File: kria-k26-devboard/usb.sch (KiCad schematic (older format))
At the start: 97 parts, among them U16 TPS2066TDGNRQ1, U17 USB7016_KDX, U18 TPS2066TDGNRQ1, U19 WE-TVS-82400152, U20 WE-TVS-82400152, U21 USB3310C-CP, U22 TPD4E05U06QDQARQ1, U23 TPD4E05U06QDQARQ1, U24 GSB3112311HR, U25 WE-TVS-82400152, U26 WE-TVS-82400152, U27 TPD4E05U06QDQARQ1, U28 TPD4E05U06QDQARQ1, U29 GSB3112311HR, Y4 ECS-2016MV-250-CN-TR3, Y5 ECS-2016MV-240-BN-TR3

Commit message: Finished PCB
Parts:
- added TP50, TP51: TP_SMD_0_75MM, antmicro-footprints:Testpoint_smd_0_75mm, symbol antmicroTestPoints:TP_SMD_0_75MM
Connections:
- net GND: no longer R62.1, R63.1
- net PS_3V3: now also R62.1, R63.1
- net at R62.2, U17.75 (PF26): now also TP50.1
- net at R63.2, U17.76 (PF27): now also TP51.1
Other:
- note added: "Slave SMBus"
- moved on the sheet: R62, R63
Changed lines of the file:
@@
 Wire Wire Line
 	2900 4400 2900 4500
-Wire Wire Line
-	7650 7400 7600 7400
-Wire Wire Line
-	7950 7400 8200 7400
 $Comp
 L antmicroResistors0402:R_200k_0402 R63
 U 1 1 64B39C27
-P 7800 7400
-F 0 "R63" H 7600 7450 60  0000 C CNN
-F 1 "R_200k_0402" H 7800 7250 60  0001 C CNN
-F 2 "antmicro-footprints:0402-res" H 8000 7600 60  0001 L CNN
-F 3 "" H 7800 7400 50  0001 C CNN
-F 4 "YAGEO_(PHYCOMP)" H 8000 7800 60  0001 L CNN "Manufacturer"
-F 5 "RC0402FR-07200KL" H 8000 7700 60  0001 L CNN "MPN"
-F 6 "200k" H 7800 7400 50  0000 C CNN "Val"
-	1    7800 7400
-	-1   0    0    1
-$EndComp
-Wire Wire Line
-	7650 7300 7600 7300
-Wire Wire Line
-	7950 7300 8200 7300
+P 8450 7050
+F 0 "R63" H 8250 7100 60  0000 C CNN
+F 1 "R_200k_0402" H 8450 6900 60  0001 C CNN
+F 2 "antmicro-footprints:0402-res" H 8650 7250 60  0001 L CNN
+F 3 "" H 8450 7050 50  0001 C CNN
+F 4 "YAGEO_(PHYCOMP)" H 8650 7450 60  0001 L CNN "Manufacturer"
+F 5 "RC0402FR-07200KL" H 8650 7350 60  0001 L CNN "MPN"
+F 6 "200k" H 8450 7050 50  0000 C CNN "Val"
+	1    8450 7050
+	0    1    1    0
+$EndComp
 $Comp
 L antmicroResistors0402:R_200k_0402 R62
 U 1 1 64B39C36
-P 7800 7300
-F 0 "R62" H 7600 7350 60  0000 C CNN
-F 1 "R_200k_0402" H 7800 7150 60  0001 C CNN
-F 2 "antmicro-footprints:0402-res" H 8000 7500 60  0001 L CNN
-F 3 "" H 7800 7300 50  0001 C CNN
-F 4 "YAGEO_(PHYCOMP)" H 8000 7700 60  0001 L CNN "Manufacturer"
-F 5 "RC0402FR-07200KL" H 8000 7600 60  0001 L CNN "MPN"
-F 6 "200k" H 7800 7300 50  0000 C CNN "Val"
-	1    7800 7300
-	-1   0    0    1
-$EndComp
-Wire Wire Line
-	8200 7300 8200 7400
-Wire Wire Line
-	8200 7600 8200 7400
-Connection ~ 8200 7400
+P 8350 7050
+F 0 "R62" H 8150 7100 60  0000 C CNN
+F 1 "R_200k_0402" H 8350 6900 60  0001 C CNN
+F 2 "antmicro-footprints:0402-res" H 8550 7250 60  0001 L CNN
+F 3 "" H 8350 7050 50  0001 C CNN
+F 4 "YAGEO_(PHYCOMP)" H 8550 7450 60  0001 L CNN "Manufacturer"
+F 5 "RC0402FR-07200KL" H 8550 7350 60  0001 L CNN "MPN"
+F 6 "200k" H 8350 7050 50  0000 C CNN "Val"
+	1    8350 7050
+	0    1    1    0
+$EndComp
 Wire Wire Line
 	8200 7700 8200 7600
@@
 	8200 7800 8200 7700
 Connection ~ 8200 7700
-Wire Wire Line
-	8200 6100 8200 7300
 Connection ~ 8200 6100
-Connection ~ 8200 7300
 Wire Wire Line
 	7600 4950 7750 4950
@@
 Wire Wire Line
 	900  2200 650  2200
-Wire Bus Line
-	10400 1100 10400 2350
 Text HLabel 7750 4950 2    50   Input ~ 0
 USB5_P
 Text HLabel 7750 5050 2    50   Input ~ 0
 USB5_N
+Text GLabel 8400 6650 1    50   Input ~ 0
+PS_3V3
+Wire Wire Line
+	8200 6100 8200 7600
+$Comp
+L antmicroTestPoints:TP_SMD_0_75MM TP50
+U 1 1 6293828A
+P 8650 7300
+F 0 "TP50" V 8750 7300 50  0000 L CNN
+F 1 "TP_SMD_0_75MM" H 8650 7200 50  0001 C CNN
+F 2 "antmicro-footprints:Testpoint_smd_0_75mm" H 8850 7500 60  0001 L CNN
+F 3 "" H 8850 7600 60  0001 L CNN
+	1    8650 7300
+	0    -1   -1   0
+$EndComp
+Wire Wire Line
+	7600 7300 8350 7300
+Wire Wire Line
+	8350 7300 8350 7200
+Wire Wire Line
+	7600 7400 8450 7400
+Wire Wire Line
+	8450 7400 8450 7200
+Wire Wire Line
+	8350 6900 8350 6700
+Wire Wire Line
+	8350 6700 8400 6700
+Wire Wire Line
+	8450 6700 8450 6900
+Wire Wire Line
+	8400 6700 8400 6650
+Connection ~ 8400 6700
+Wire Wire Line
+	8400 6700 8450 6700
+$Comp
+L antmicroTestPoints:TP_SMD_0_75MM TP51
+U 1 1 62D35A30
+P 8650 7400
+F 0 "TP51" V 8550 7400 50  0000 L CNN
+F 1 "TP_SMD_0_75MM" H 8650 7300 50  0001 C CNN
+F 2 "antmicro-footprints:Testpoint_smd_0_75mm" H 8850 7600 60  0001 L CNN
+F 3 "" H 8850 7700 60  0001 L CNN
+	1    8650 7400
+	0    -1   -1   0
+$EndComp
+Wire Wire Line
+	8350 7300 8550 7300
+Connection ~ 8350 7300
+Wire Wire Line
+	8450 7400 8550 7400
+Wire Bus Line
+	10400 1100 10400 2350
+Connection ~ 8450 7400
+Text Notes 8350 7650 0    50   ~ 0
+Slave SMBus
 $EndSCHEMATC

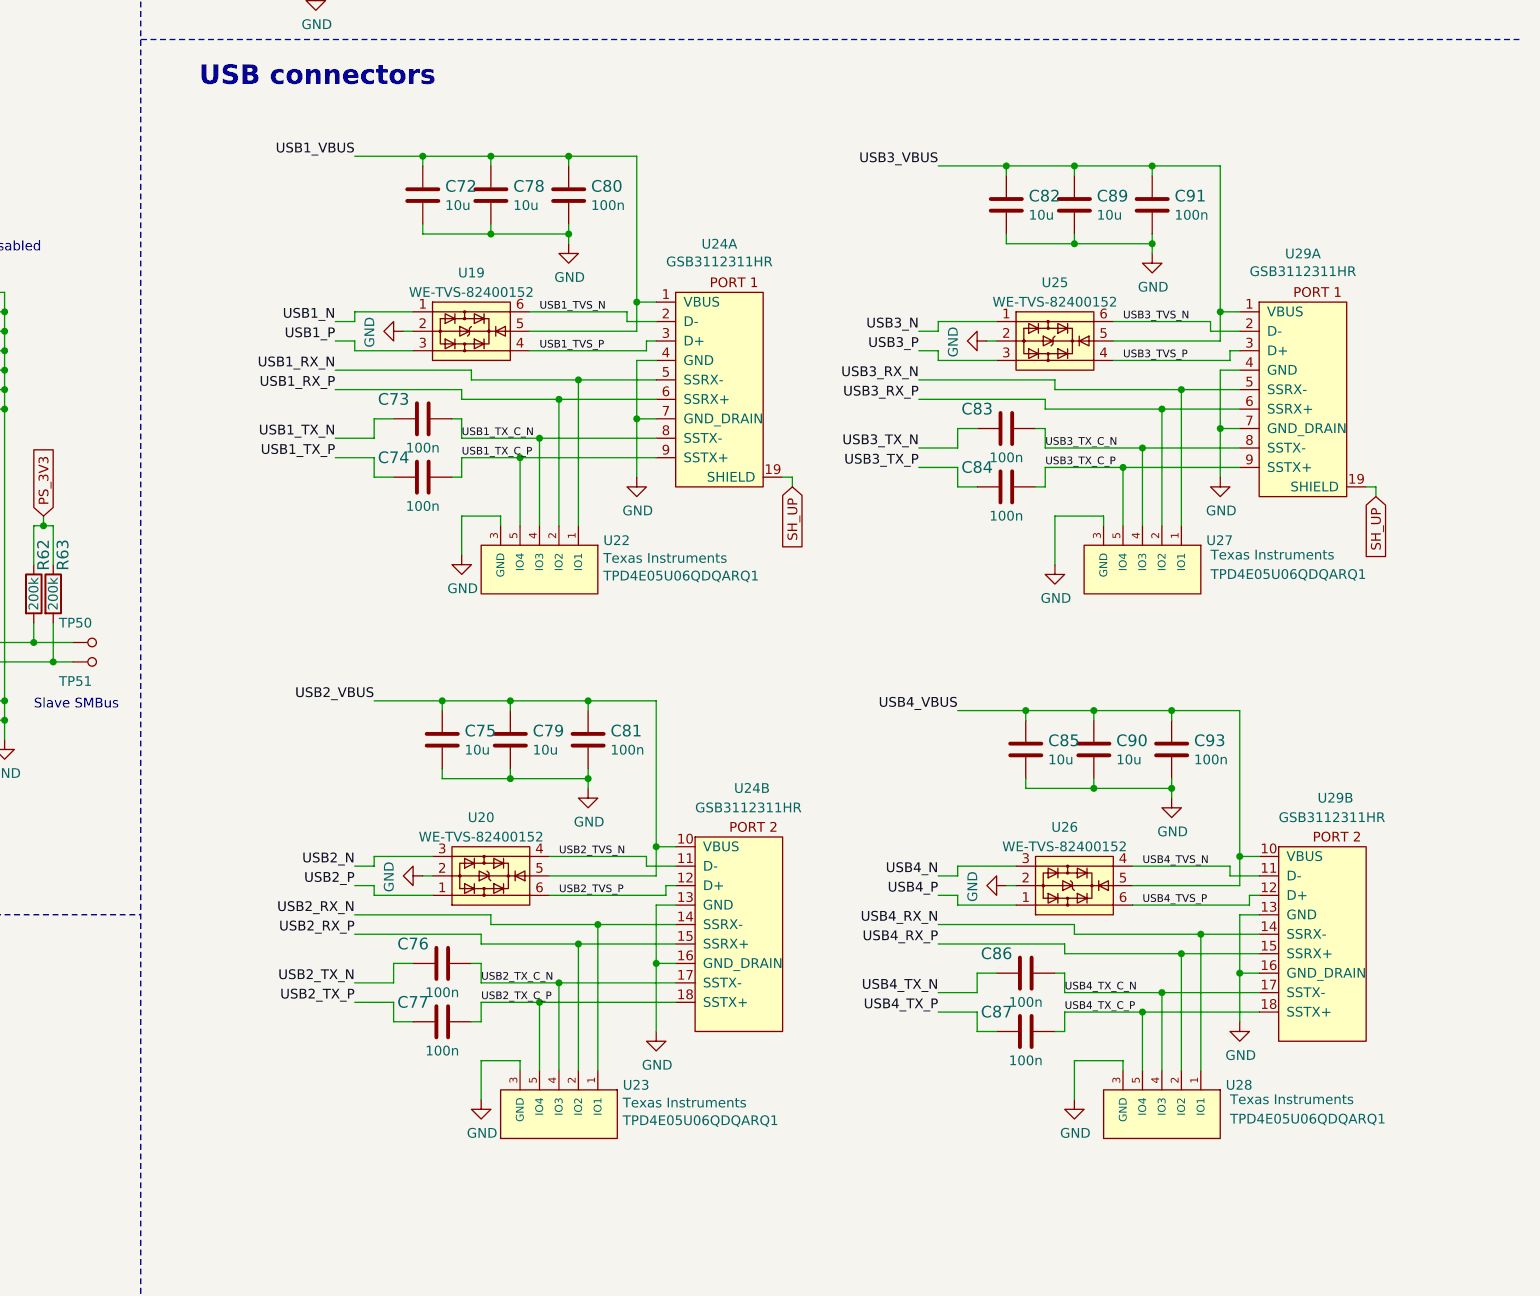
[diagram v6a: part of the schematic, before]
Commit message: Modified TPD4E05U06QDQARQ1 symbol to avoid misconnections on the schematic
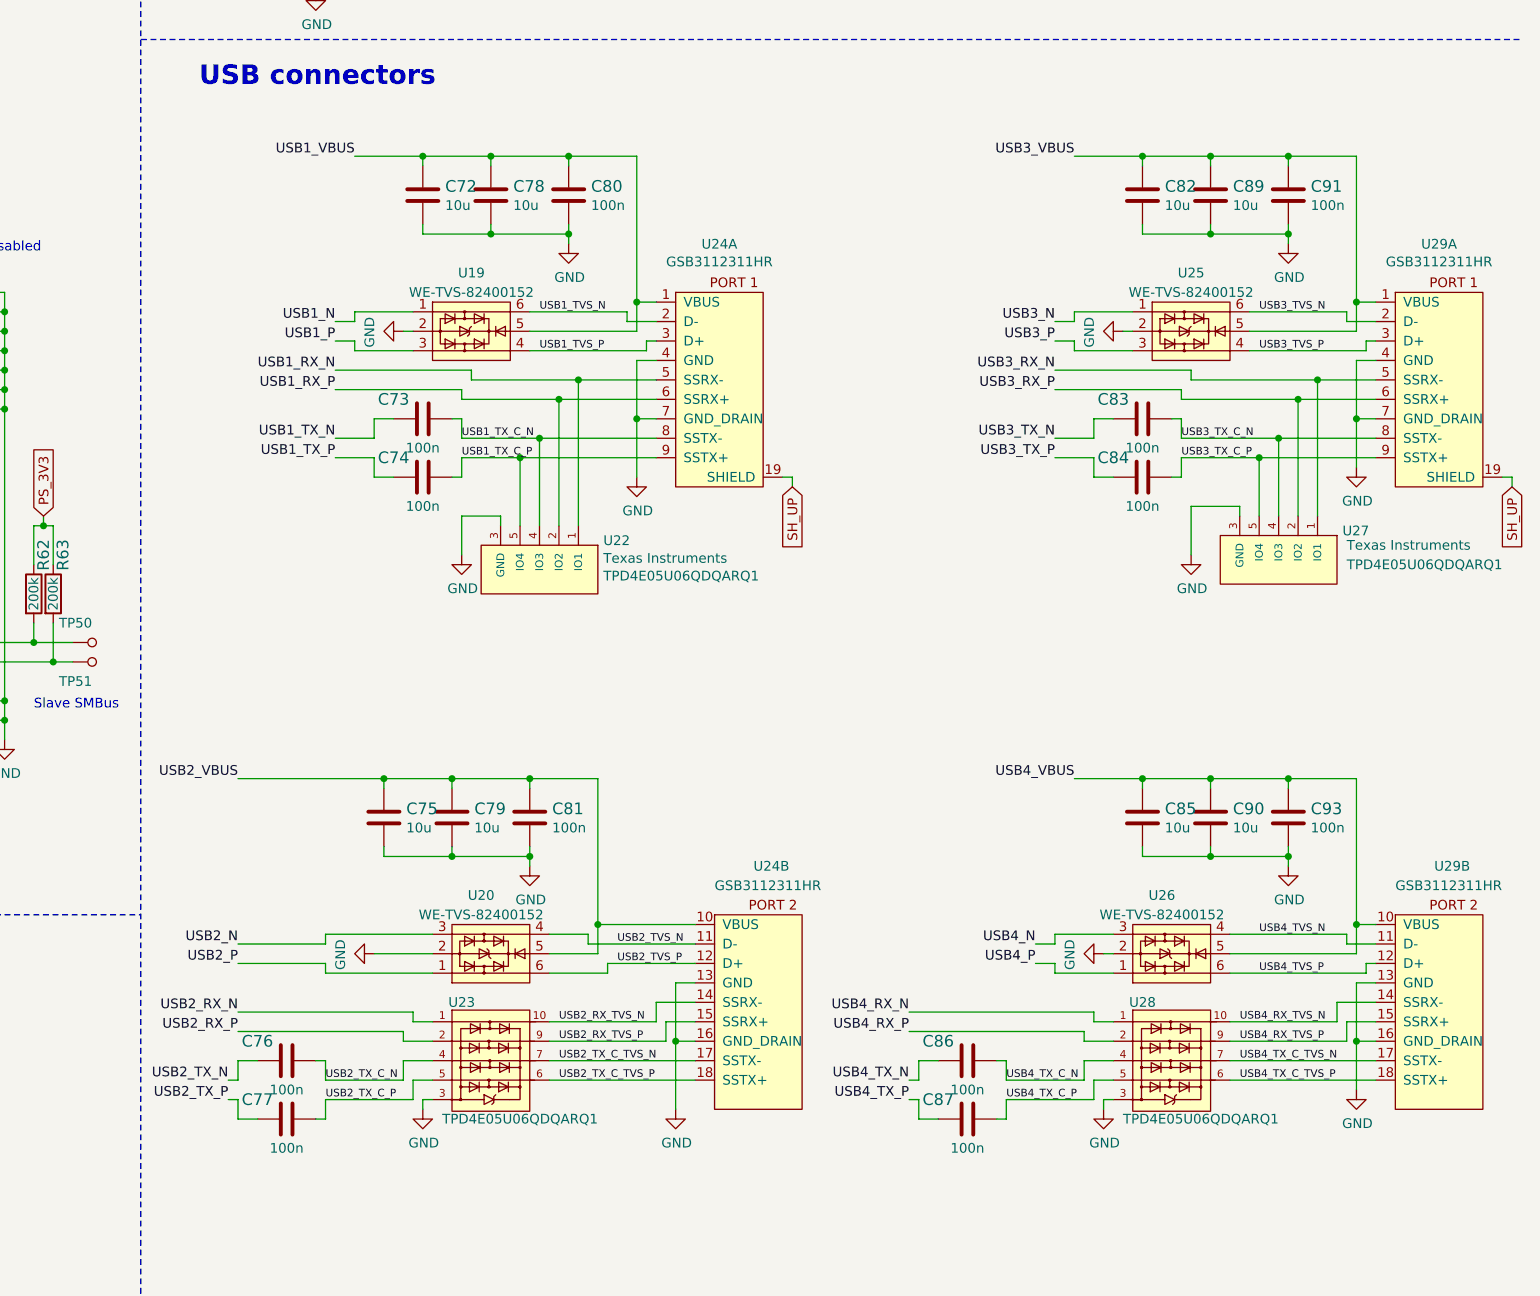
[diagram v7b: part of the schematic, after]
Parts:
- removed U23, U28: TPD4E05U06QDQARQ1, antmicro-footprints:TPD4E05U06QDQARQ1, symbol antmicroTVSDiodes:TPD4E05U06QDQARQ1
- added U23, U28: TPD4E05U06QDQARQ1_PASS, antmicro-footprints:TPD4E05U06QDQARQ1, symbol antmicroTVSDiodes:TPD4E05U06QDQARQ1_PASS
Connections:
- net GND: now also U23.3, U23.8 (GND), U28.3, U28.8 (GND)
- net USB2_RX_N: now also U23.1; no longer U24.14 (SSRX-)
- net USB2_RX_P: now also U23.2; no longer U24.15 (SSRX+)
- net USB2_TX_C_N: now also U23.4; no longer U24.17 (SSTX-)
- net USB2_TX_C_P: now also U23.5; no longer U24.18 (SSTX+)
- net USB4_RX_N: now also U28.1; no longer U29.14 (SSRX-)
- net USB4_RX_P: now also U28.2; no longer U29.15 (SSRX+)
- net USB4_TX_C_N: now also U28.4; no longer U29.17 (SSTX-)
- net USB4_TX_C_P: now also U28.5; no longer U29.18 (SSTX+)
- new net USB2_RX_TVS_N: U23.10, U24.14 (SSRX-)
- new net USB2_RX_TVS_P: U23.9, U24.15 (SSRX+)
- new net USB2_TX_C_TVS_N: U23.7, U24.17 (SSTX-)
- new net USB2_TX_C_TVS_P: U23.6, U24.18 (SSTX+)
- new net USB4_RX_TVS_N: U28.10, U29.14 (SSRX-)
- new net USB4_RX_TVS_P: U28.9, U29.15 (SSRX+)
- new net USB4_TX_C_TVS_N: U28.7, U29.17 (SSTX-)
- new net USB4_TX_C_TVS_P: U28.6, U29.18 (SSTX+)
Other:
- moved on the sheet: C75, C76, C77, C79, C81, C82, C83, C84, C85, C86, C87, C89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

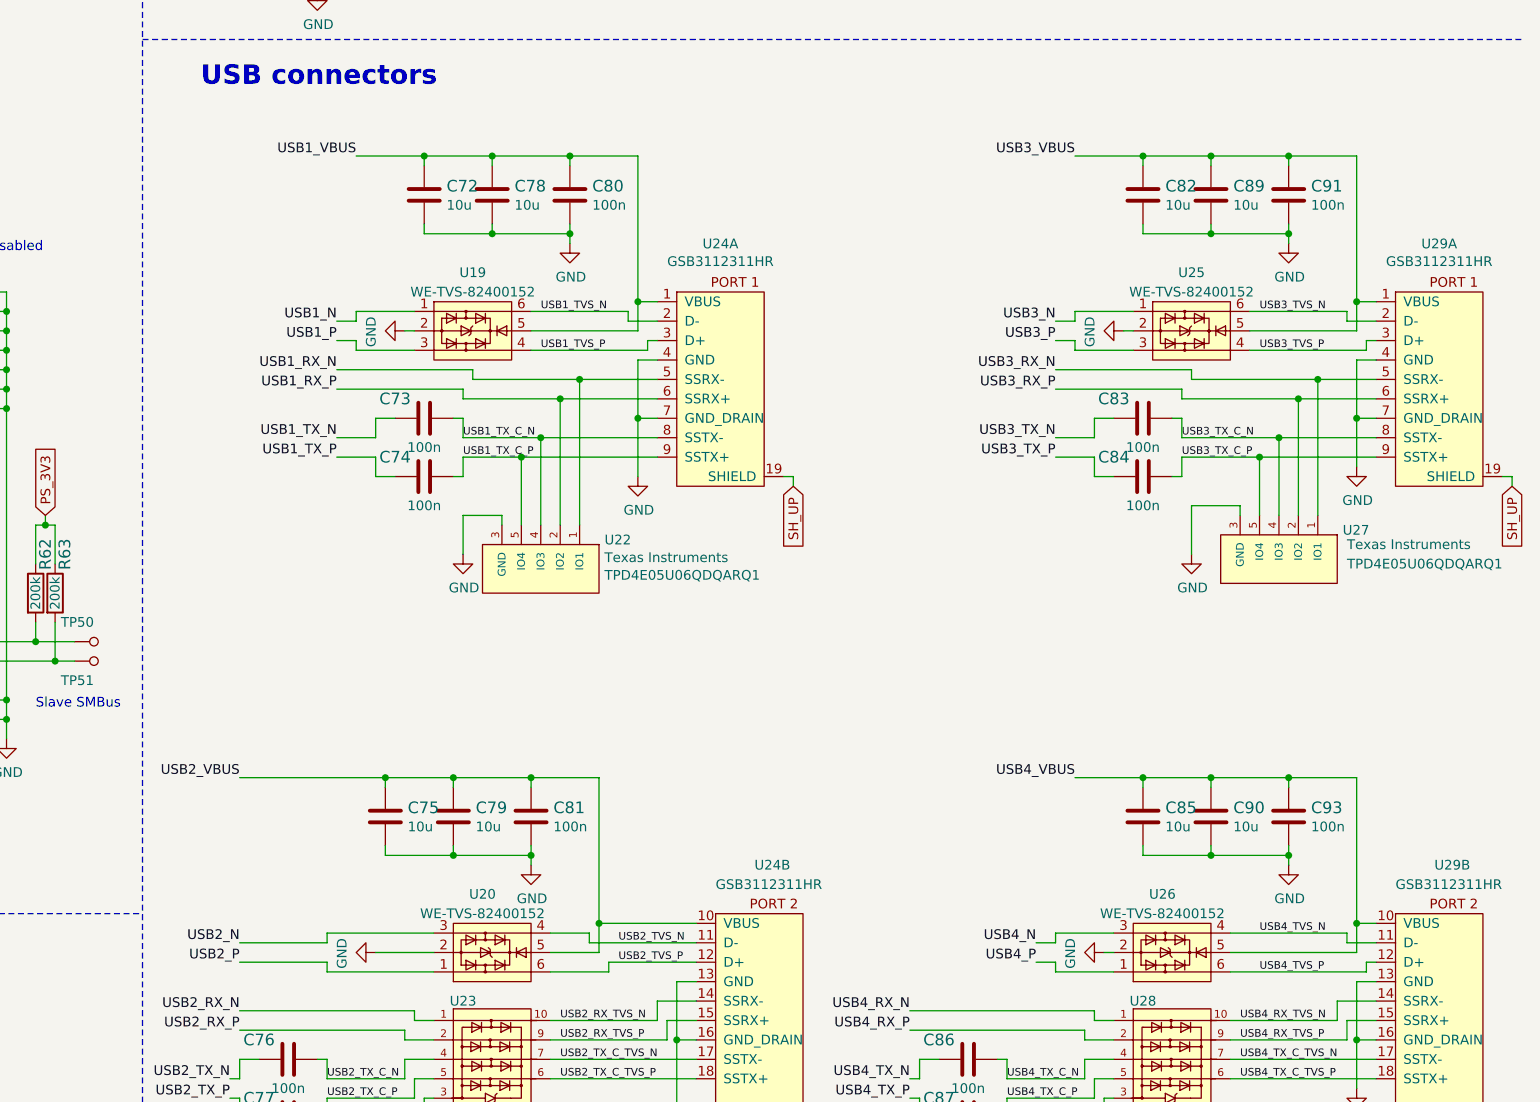
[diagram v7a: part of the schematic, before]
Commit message: Fixes introduced after initial review, length matching double checked with external plugin
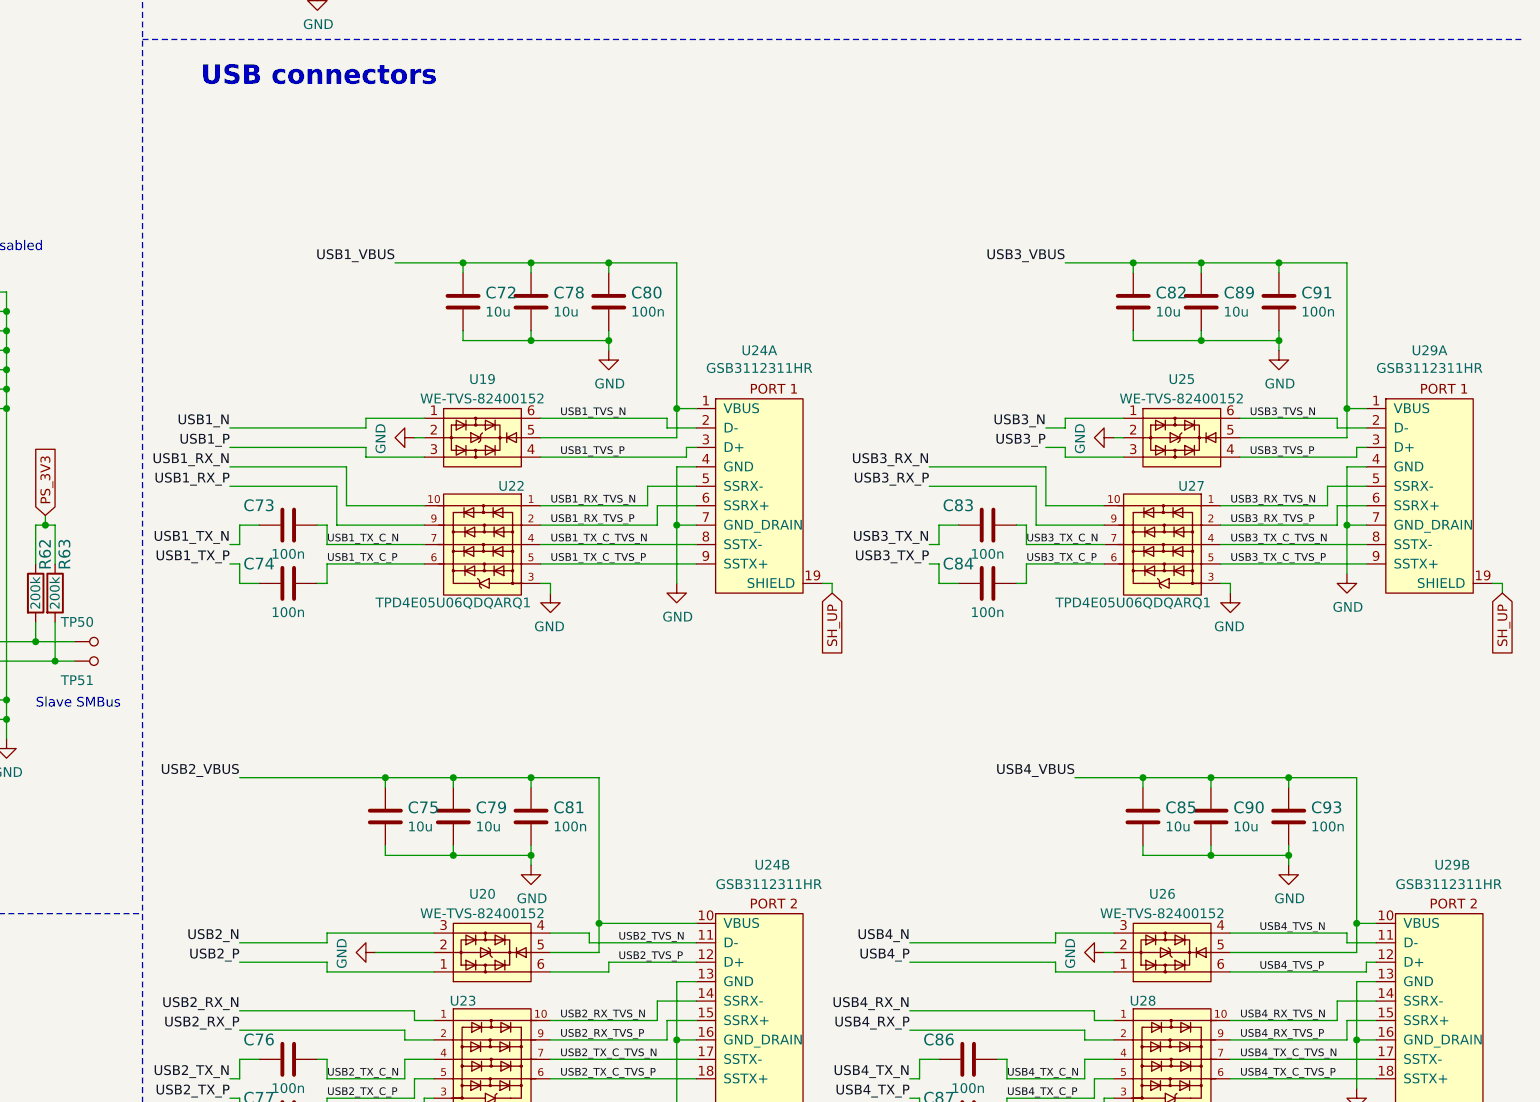
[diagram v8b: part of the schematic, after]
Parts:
- removed U22, U27: TPD4E05U06QDQARQ1, antmicro-footprints:TPD4E05U06QDQARQ1, symbol antmicroTVSDiodes:TPD4E05U06QDQARQ1
- added U22, U27: TPD4E05U06QDQARQ1_PASS, antmicro-footprints:TPD4E05U06QDQARQ1, symbol antmicroTVSDiodes:TPD4E05U06QDQARQ1_PASS
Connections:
- net GND: now also U22.3, U22.8 (GND), U27.3, U27.8 (GND)
- net USB1_RX_N: now also U22.10; no longer U24.5 (SSRX-)
- net USB1_RX_P: now also U22.9; no longer U24.6 (SSRX+)
- net USB1_TX_C_N: now also U22.7; no longer U24.8 (SSTX-)
- net USB1_TX_C_P: now also U22.6; no longer U24.9 (SSTX+)
- net USB3_RX_N: now also U27.10; no longer U29.5 (SSRX-)
- net USB3_RX_P: now also U27.9; no longer U29.6 (SSRX+)
- net USB3_TX_C_N: now also U27.7; no longer U29.8 (SSTX-)
- net USB3_TX_C_P: now also U27.6; no longer U29.9 (SSTX+)
- new net USB1_RX_TVS_N: U22.1, U24.5 (SSRX-)
- new net USB1_RX_TVS_P: U22.2, U24.6 (SSRX+)
- new net USB1_TX_C_TVS_N: U22.4, U24.8 (SSTX-)
- new net USB1_TX_C_TVS_P: U22.5, U24.9 (SSTX+)
- new net USB3_RX_TVS_N: U27.1, U29.5 (SSRX-)
- new net USB3_RX_TVS_P: U27.2, U29.6 (SSRX+)
- new net USB3_TX_C_TVS_N: U27.4, U29.8 (SSTX-)
- new net USB3_TX_C_TVS_P: U27.5, U29.9 (SSTX+)
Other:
- moved on the sheet: C72, C73, C74, C78, C80, C82, C83, C84, C89, C91, U19, U24A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
